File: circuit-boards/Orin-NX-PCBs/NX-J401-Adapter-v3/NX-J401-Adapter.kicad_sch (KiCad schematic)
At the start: 15 parts, among them J1 18V_OUT, J3 CAN-NX, J5 NX-BUTTON, J6 CAN-NX, J7 CAN-NX, J8 CONSOLE, J9 Power, SW1 RESET, SW2 RECOVERY

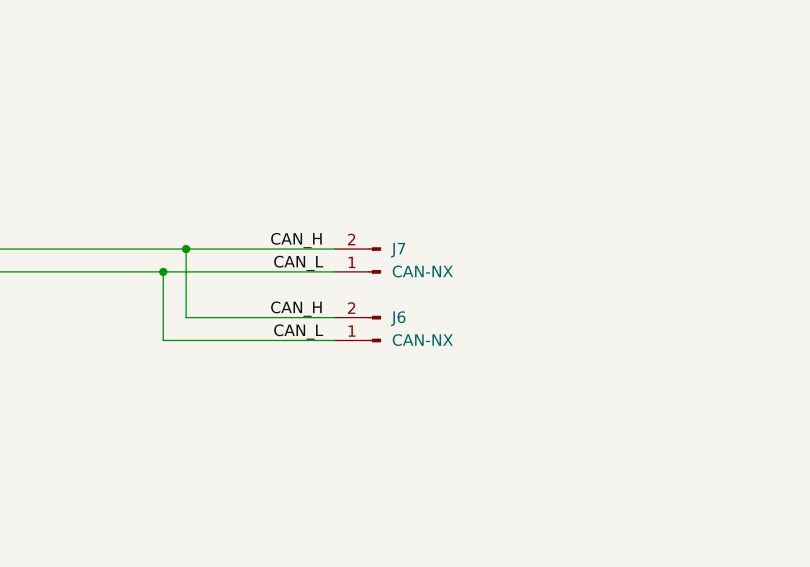
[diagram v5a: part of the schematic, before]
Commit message: minor update to boost converter layout
Signed-off-by: Scott Berman <scott.berman@bluerivertech.com>
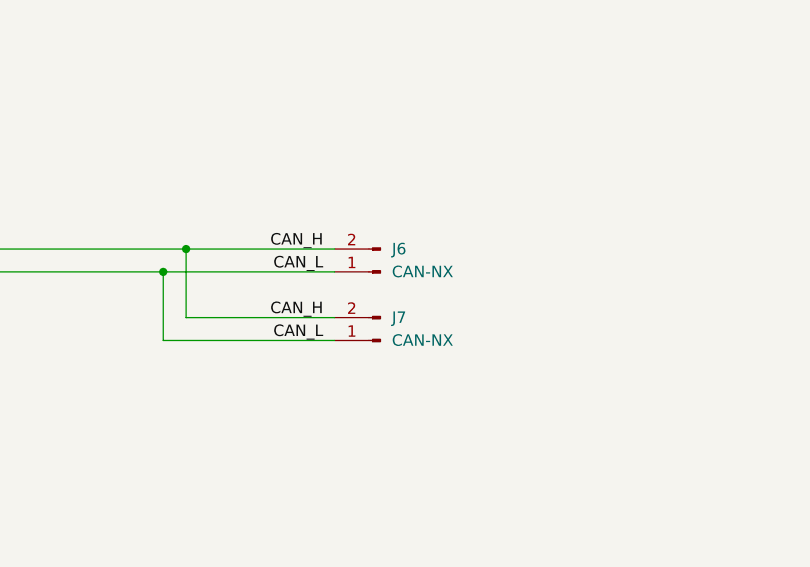
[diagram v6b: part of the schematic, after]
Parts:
- renumbered J7 to J6, J6 to J7
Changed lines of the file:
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@@
 		(on_board yes)
 		(dnp no)
-		(property "Reference" "J6"
+		(property "Reference" "J7"
 			(at 302.26 163.83 0)
 			(effects
@@
 			(project "NX-J401-Adapter"
 				(path "/cc31ce4b-09ab-4aea-a1d3-ed84696ba658"
-					(reference "J6")
+					(reference "J7")
 					(unit 1)
 				)
@@
 		(on_board yes)
 		(dnp no)
-		(property "Reference" "J7"
+		(property "Reference" "J6"
 			(at 302.26 156.21 0)
 			(effects
@@
 			(project "NX-J401-Adapter"
 				(path "/cc31ce4b-09ab-4aea-a1d3-ed84696ba658"
-					(reference "J7")
-					(unit 1)
-				)
+					(reference "J6")
+					(unit 1)
+				)
